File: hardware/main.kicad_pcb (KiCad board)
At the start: 2 copper layers, 84.6 x 84.6 mm, 130 parts, among them J1 USB_DEBUG, J2 USB_TO_ANDROID, M1 Mounting Hole, M2 Mounting Hole, M3 Mounting Hole, M4 Mounting Hole, P1 VBAT-TEST, P11 MOTOR-R, P12 MOTOR-L, P13 AND5V, P14 P24, P2 USB-VBUS, P3 SERVO-TILT, P4 JTAG10, P5 POWER-CHARGE, P6 POWER, P7 BATCHG, P8 12VIN, P9 BAT, Q1 ZXMP2120FFTA, Q2 BD242CG, Q3 IRLML2803TRPBF, Q4 IRLML2803TRPBF, U1 STM32F102C6, U2 BQ24450, U3 ZLDO1117, U4 AP6502, U5 7408, U6 MC33926, U7 MC33926, U8 FT312D, X1 8MHz, X2 12MHz

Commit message: v1 update
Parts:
- P4: footprint HDRV10W66P254_2X5_1270X503X838P -> SHDRV10W66P254_2X5_2035X870X609P
- moved C41 5.46 mm to (174.2, 70.4)
- moved C39 0.20 mm to (176.6, 70.4)
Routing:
- net N-00000111: track 12.9 -> 13.6 mm
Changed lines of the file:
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@@
     (thickness 1.6)
     (drawings 49)
-    (tracks 1374)
+    (tracks 1376)
     (zones 0)
     (modules 130)
@@
   (module CAPC2012X100N (layer F.Cu)
     (at 150.8 71.6 270)
-    (fp_text reference C16 (at 0.4 -1.6 270) (layer F.SilkS)
+    (fp_text reference C16 (at -2.2 0 360) (layer F.SilkS)
       (effects (font (size 0.5 0.5) (thickness 0.1)))
     )
@@
   )
   (module CAPC2012X100N (layer F.Cu)
-    (at 176.4 70.4 270)
-    (fp_text reference C39 (at 0 1.5 270) (layer F.SilkS)
+    (at 176.6 70.4 270)
+    (fp_text reference C39 (at 2.2 0.2 360) (layer F.SilkS)
       (effects (font (size 0.5 0.5) (thickness 0.1)))
     )
@@
   )
   (module CAPC2012X100N (layer F.Cu)
-    (at 172 75.4 90)
-    (fp_text reference C41 (at 2.2 -0.2 180) (layer F.SilkS)
+    (at 174.2 70.4 90)
+    (fp_text reference C41 (at -2.2 0.2 180) (layer F.SilkS)
       (effects (font (size 0.5 0.5) (thickness 0.1)))
     )
@@
     )
   )
-  (module HDRV10W66P254_2X5_1270X503X838P (layer F.Cu)
-    (at 167.64 73.66 180)
-    (fp_text reference P4 (at 12.24 -1.34 270) (layer F.SilkS)
-      (effects (font (size 1 1) (thickness 0.15)))
-    )
-    (fp_text value JTAG10 (at 1.27 0 180) (layer F.SilkS)
-      (effects (font (size 1 1) (thickness 0.15)))
-    )
-    (fp_line (start -1.4 -3.9) (end 11.6 -3.9) (layer Cmts.User) (width 0.1))
-    (fp_line (start 11.6 -3.9) (end 11.6 1.4) (layer Cmts.User) (width 0.1))
-    (fp_line (start 11.6 1.4) (end -1.4 1.4) (layer Cmts.User) (width 0.1))
-    (fp_line (start -1.4 1.4) (end -1.4 -3.9) (layer Cmts.User) (width 0.1))
-    (fp_line (start -1.25 -3.75) (end 11.45 -3.75) (layer F.SilkS) (width 0.1))
-    (fp_line (start 11.45 -3.75) (end 11.45 1.25) (layer F.SilkS) (width 0.1))
-    (fp_line (start 11.45 1.25) (end -1.25 1.25) (layer F.SilkS) (width 0.1))
-    (fp_line (start -1.25 1.25) (end -1.25 -3.75) (layer F.SilkS) (width 0.1))
-    (pad 1 thru_hole rect (at 0 0 180) (size 1.65 1.65) (drill 1)
-      (layers *.Cu *.Mask F.SilkS)
-      (net 30 /JTCK)
-    )
-    (pad 2 thru_hole circle (at 0 -2.54 180) (size 1.65 1.65) (drill 1)
-      (layers *.Cu *.Mask F.SilkS)
-      (net 48 GND)
-    )
-    (pad 3 thru_hole circle (at 2.54 0 180) (size 1.65 1.65) (drill 1)
-      (layers *.Cu *.Mask F.SilkS)
-      (net 32 /JTDO)
-    )
-    (pad 4 thru_hole circle (at 2.54 -2.54 180) (size 1.65 1.65) (drill 1)
-      (layers *.Cu *.Mask F.SilkS)
-      (net 3 +3.3V)
-    )
-    (pad 5 thru_hole circle (at 5.08 0 180) (size 1.65 1.65) (drill 1)
-      (layers *.Cu *.Mask F.SilkS)
-      (net 33 /JTMS)
-    )
-    (pad 6 thru_hole circle (at 5.08 -2.54 180) (size 1.65 1.65) (drill 1)
-      (layers *.Cu *.Mask F.SilkS)
-      (net 47 /nRST)
-    )
-    (pad 7 thru_hole circle (at 7.62 0 180) (size 1.65 1.65) (drill 1)
-      (layers *.Cu *.Mask F.SilkS)
-      (net 84 N-0000030)
-    )
-    (pad 8 thru_hole circle (at 7.62 -2.54 180) (size 1.65 1.65) (drill 1)
-      (layers *.Cu *.Mask F.SilkS)
-      (net 29 /JNTRST)
-    )
-    (pad 9 thru_hole circle (at 10.16 0 180) (size 1.65 1.65) (drill 1)
-      (layers *.Cu *.Mask F.SilkS)
-      (net 31 /JTDI)
-    )
-    (pad 10 thru_hole circle (at 10.16 -2.54 180) (size 1.65 1.65) (drill 1)
-      (layers *.Cu *.Mask F.SilkS)
-      (net 90 N-0000057)
-    )
-  )
   (module HDRV4W66P254_1X4_1016X249X838P (layer F.Cu)
     (at 157 57.8)
@@
   (module RESC2012X100N (layer F.Cu)
     (at 159.5 80.9 180)
-    (fp_text reference R44 (at 0.9 1.5 180) (layer F.SilkS)
+    (fp_text reference R44 (at 2.1 -0.1 270) (layer F.SilkS)
       (effects (font (size 0.5 0.5) (thickness 0.1)))
     )
@@
     )
   )
+  (module SHDRV10W66P254_2X5_2035X870X609P (layer F.Cu)
+    (at 167.64 73.66 180)
+    (fp_text reference P4 (at 14.24 -6.74 180) (layer F.SilkS)
+      (effects (font (size 1 1) (thickness 0.15)))
+    )
+    (fp_text value JTAG10 (at 1.27 0 180) (layer F.SilkS)
+      (effects (font (size 1 1) (thickness 0.15)))
+    )
+    (fp_line (start 7.23 1.98) (end 7.23 3.08) (layer F.SilkS) (width 0.1))
+    (fp_line (start 2.93 1.98) (end 2.93 3.08) (layer F.SilkS) (width 0.1))
+    (fp_line (start -3.995 1.98) (end -3.995 -4.52) (layer F.SilkS) (width 0.1))
+    (fp_line (start -3.995 -4.52) (end 14.155 -4.52) (layer F.SilkS) (width 0.1))
+    (fp_line (start 14.155 -4.52) (end 14.155 1.98) (layer F.SilkS) (width 0.1))
+    (fp_line (start -3.995 1.98) (end 14.155 1.98) (layer F.SilkS) (width 0.1))
+    (fp_line (start -5.345 -5.87) (end 15.505 -5.87) (layer Cmts.User) (width 0.1))
+    (fp_line (start 15.505 -5.87) (end 15.505 3.33) (layer Cmts.User) (width 0.1))
+    (fp_line (start 15.505 3.33) (end -5.345 3.33) (layer Cmts.User) (width 0.1))
+    (fp_line (start -5.345 3.33) (end -5.345 -5.87) (layer Cmts.User) (width 0.1))
+    (fp_line (start -5.095 -5.62) (end 15.255 -5.62) (layer F.SilkS) (width 0.1))
+    (fp_line (start 15.255 -5.62) (end 15.255 3.08) (layer F.SilkS) (width 0.1))
+    (fp_line (start 15.255 3.08) (end -5.095 3.08) (layer F.SilkS) (width 0.1))
+    (fp_line (start -5.095 3.08) (end -5.095 -5.62) (layer F.SilkS) (width 0.1))
+    (pad 1 thru_hole rect (at 0 0 180) (size 1.65 1.65) (drill 1)
+      (layers *.Cu *.Mask F.SilkS)
+      (net 30 /JTCK)
+    )
+    (pad 2 thru_hole circle (at 0 -2.54 180) (size 1.65 1.65) (drill 1)
+      (layers *.Cu *.Mask F.SilkS)
+      (net 48 GND)
+    )
+    (pad 3 thru_hole circle (at 2.54 0 180) (size 1.65 1.65) (drill 1)
+      (layers *.Cu *.Mask F.SilkS)
+      (net 32 /JTDO)
+    )
+    (pad 4 thru_hole circle (at 2.54 -2.54 180) (size 1.65 1.65) (drill 1)
+      (layers *.Cu *.Mask F.SilkS)
+      (net 3 +3.3V)
+    )
+    (pad 5 thru_hole circle (at 5.08 0 180) (size 1.65 1.65) (drill 1)
+      (layers *.Cu *.Mask F.SilkS)
+      (net 33 /JTMS)
+    )
+    (pad 6 thru_hole circle (at 5.08 -2.54 180) (size 1.65 1.65) (drill 1)
+      (layers *.Cu *.Mask F.SilkS)
+      (net 47 /nRST)
+    )
+    (pad 7 thru_hole circle (at 7.62 0 180) (size 1.65 1.65) (drill 1)
+      (layers *.Cu *.Mask F.SilkS)
+      (net 84 N-0000030)
+    )
+    (pad 8 thru_hole circle (at 7.62 -2.54 180) (size 1.65 1.65) (drill 1)
+      (layers *.Cu *.Mask F.SilkS)
+      (net 29 /JNTRST)
+    )
+    (pad 9 thru_hole circle (at 10.16 0 180) (size 1.65 1.65) (drill 1)
+      (layers *.Cu *.Mask F.SilkS)
+      (net 31 /JTDI)
+    )
+    (pad 10 thru_hole circle (at 10.16 -2.54 180) (size 1.65 1.65) (drill 1)
+      (layers *.Cu *.Mask F.SilkS)
+      (net 90 N-0000057)
+    )
+  )
   (gr_text VBAT-TEST (at 147.6 106.2) (layer F.SilkS)
     (effects (font (size 0.5 0.5) (thickness 0.12)))
@@
     (effects (font (size 0.5 0.5) (thickness 0.12)))
   )
-  (gr_text JTAG (at 162 71.2) (layer F.SilkS)
+  (gr_text JTAG (at 151.4 77.8 90) (layer F.SilkS)
     (effects (font (size 1 1) (thickness 0.2)))
   )
@@
   (segment (start 131.95 117.35) (end 132.2 117.35) (width 0.2032) (layer F.Cu) (net 2))
   (segment (start 130.05 115.45) (end 131.95 117.35) (width 0.2032) (layer F.Cu) (net 2))
+  (segment (start 176.4 67) (end 176.4 69.25) (width 0.2032) (layer F.Cu) (net 3))
+  (segment (start 176.4 69.25) (end 176.6 69.45) (width 0.2032) (layer F.Cu) (net 3))
   (segment (start 139.55 109.2) (end 140.2 109.2) (width 0.2032) (layer F.Cu) (net 3))
   (segment (start 140.4 109.2) (end 141 108.6) (width 0.2032) (layer F.Cu) (net 3))
@@
   (segment (start 182.6 65.6) (end 180.8 65.6) (width 0.2032) (layer F.Cu) (net 3))
   (segment (start 180.8 65.6) (end 178.2 63) (width 0.2032) (layer F.Cu) (net 3))
-  (segment (start 176.4 67) (end 176.4 69.45) (width 0.2032) (layer F.Cu) (net 3))
   (segment (start 182.6 62.4) (end 178.8 62.4) (width 0.2032) (layer F.Cu) (net 3))
   (segment (start 178.8 62.4) (end 178.2 63) (width 0.2032) (layer F.Cu) (net 3))
@@
   (segment (start 161.65 113.55) (end 161.65 111.8) (width 0.2032) (layer F.Cu) (net 47))
   (segment (start 158.1 115.15) (end 151.9 115.15) (width 0.2032) (layer F.Cu) (net 47))
+  (segment (start 175.6 67) (end 173.8 67) (width 0.2032) (layer F.Cu) (net 48))
+  (via (at 173 67.8) (size 0.889) (layers F.Cu B.Cu) (net 48))
+  (segment (start 173.8 67) (end 173 67.8) (width 0.2032) (layer F.Cu) (net 48))
   (segment (start 148.35 45.2) (end 149.8 45.2) (width 0.2032) (layer F.Cu) (net 48))
   (via (at 149.8 45.2) (size 0.889) (layers F.Cu B.Cu) (net 48))
@@
   (via (at 146 104.8) (size 0.889) (layers F.Cu B.Cu) (net 48))
   (segment (start 146.75 104.05) (end 146 104.8) (width 0.2032) (layer F.Cu) (net 48))
-  (segment (start 175.6 67) (end 175.2 67) (width 0.2032) (layer F.Cu) (net 48))
-  (via (at 173.6 68.6) (size 0.889) (layers F.Cu B.Cu) (net 48))
-  (segment (start 175.2 67) (end 173.6 68.6) (width 0.2032) (layer F.Cu) (net 48))
   (segment (start 158.55 83.2) (end 157 83.2) (width 0.2032) (layer F.Cu) (net 48))
   (via (at 157 83.2) (size 0.889) (layers F.Cu B.Cu) (net 48))
@@
   (via (at 134.4 91.4) (size 0.889) (layers F.Cu B.Cu) (net 58))
   (segment (start 133.85 90.85) (end 134.4 91.4) (width 0.254) (layer F.Cu) (net 58))
-  (segment (start 172 76.35) (end 173.85 76.35) (width 0.2032) (layer F.Cu) (net 59))
-  (segment (start 173.85 76.35) (end 175 75.2) (width 0.2032) (layer F.Cu) (net 59))
+  (segment (start 175 75.2) (end 175 74) (width 0.2032) (layer F.Cu) (net 59))
+  (segment (start 174.2 73.2) (end 174.2 71.35) (width 0.2032) (layer F.Cu) (net 59))
+  (segment (start 175 74) (end 174.2 73.2) (width 0.2032) (layer F.Cu) (net 59))
   (segment (start 178 67) (end 178 72.2) (width 0.2032) (layer F.Cu) (net 59))
   (segment (start 178 72.2) (end 175 75.2) (width 0.2032) (layer F.Cu) (net 59))

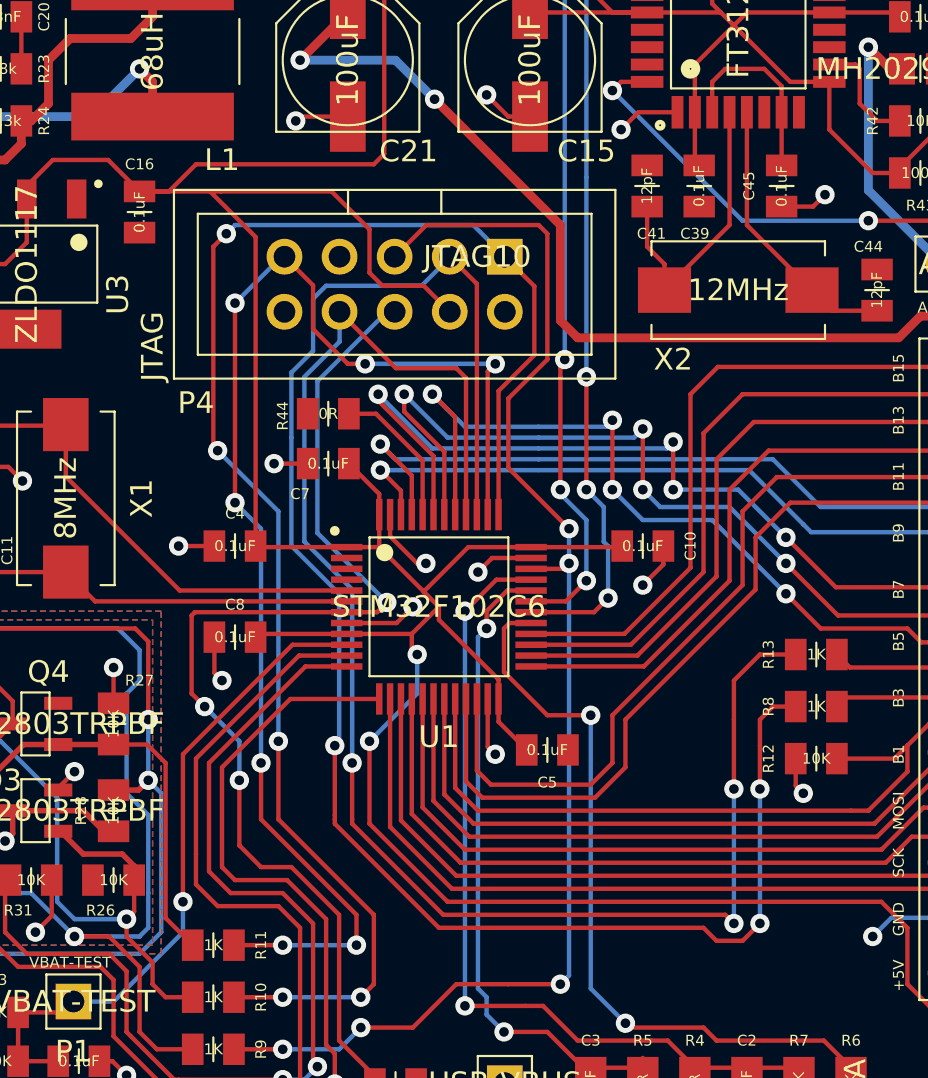
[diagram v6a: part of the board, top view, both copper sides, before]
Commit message: rotated jtag header
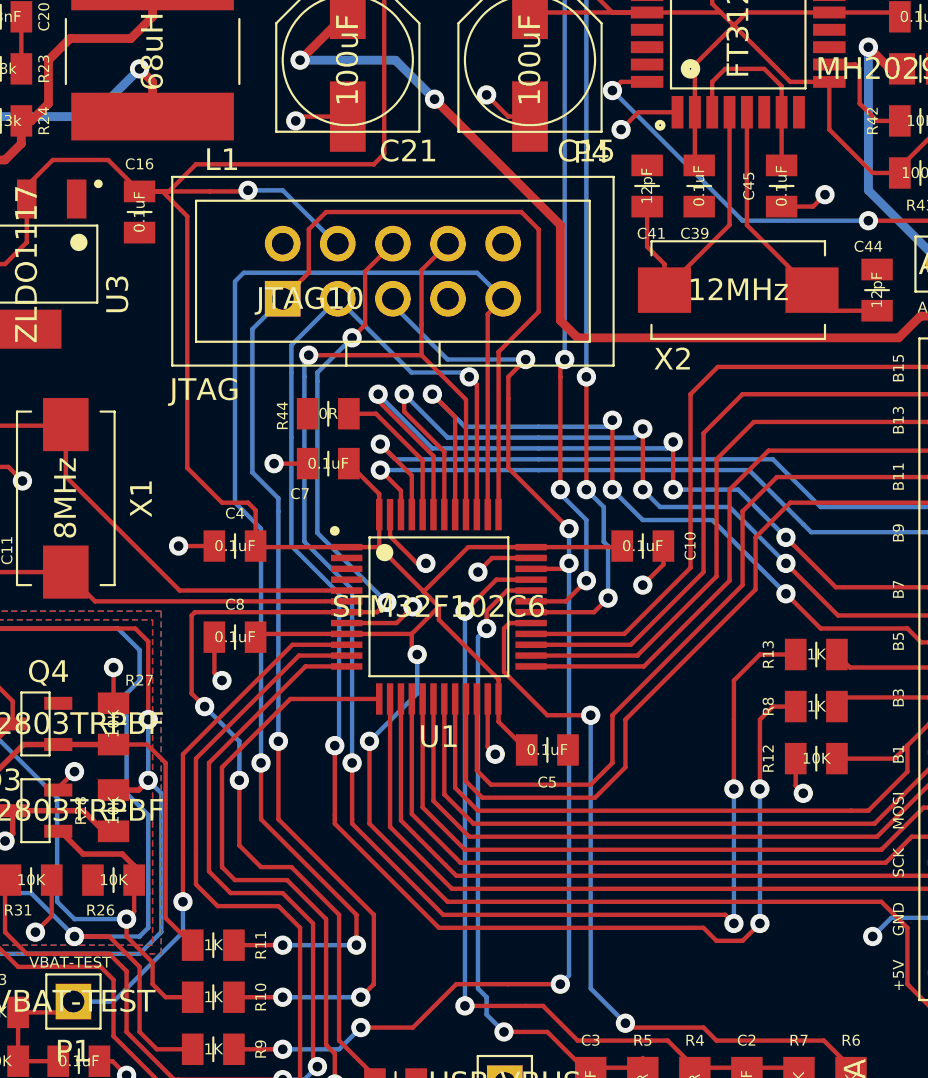
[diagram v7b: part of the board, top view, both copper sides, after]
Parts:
- moved P4 10.4 mm to (157.4, 75.6), turned to 0 degrees
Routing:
- net /JTMS: track 62.6 -> 56.4 mm, vias 5 -> 6
- net /JTDO: track 78.6 -> 73.6 mm, vias 3 -> 4
- net +3.3V: track 365.5 -> 360.6 mm, vias 7 -> 8
- net /JNTRST: track 72.6 -> 75.7 mm, vias 3 -> 4
- net /nRST: track 64.1 -> 67.0 mm, vias 5 -> 6
- net /JTCK: track 71.4 -> 70.1 mm, vias 5 -> 3
- net /JTDI: track 60.8 -> 61.8 mm, vias 7 -> 3
